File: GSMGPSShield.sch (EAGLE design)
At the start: 65 parts, among them IC1 RT8289, IC2 SIM900, J1 SIM Socket, J2 Antenna, J3 Breakout 1, J4 Breakout 2, J5 ARDUINO-SHIELD_R3, Q1 2N7002, Q2 2N7002, Q3 2N7002, Q4 2N7002, Q5 2N7002

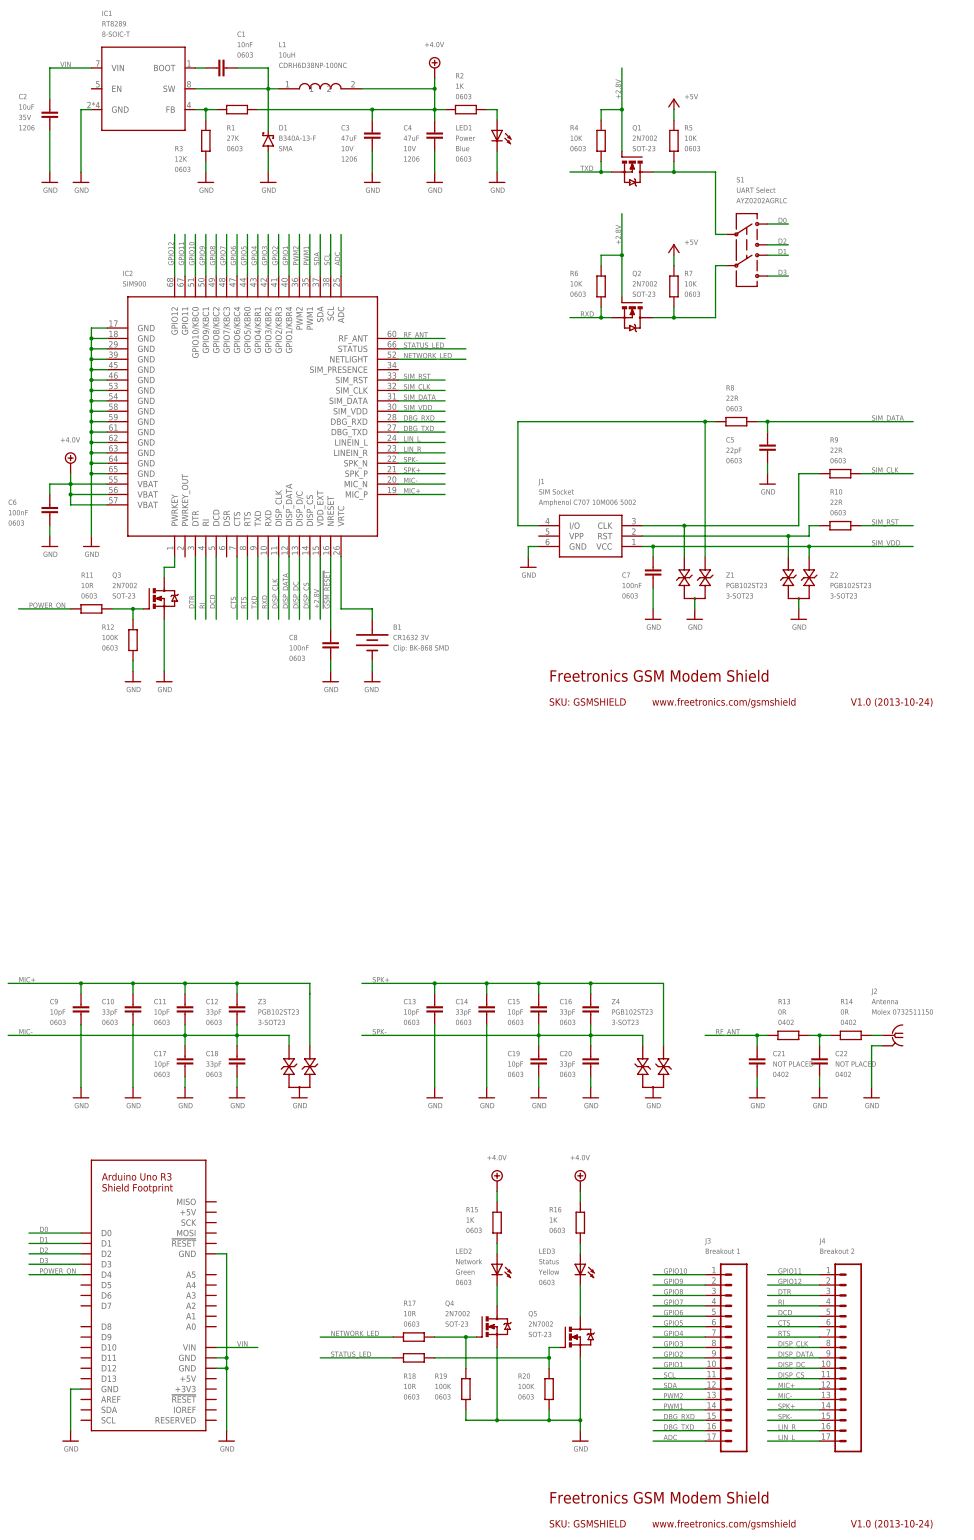
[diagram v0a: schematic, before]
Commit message: changed to SIM908 module, first finished draft
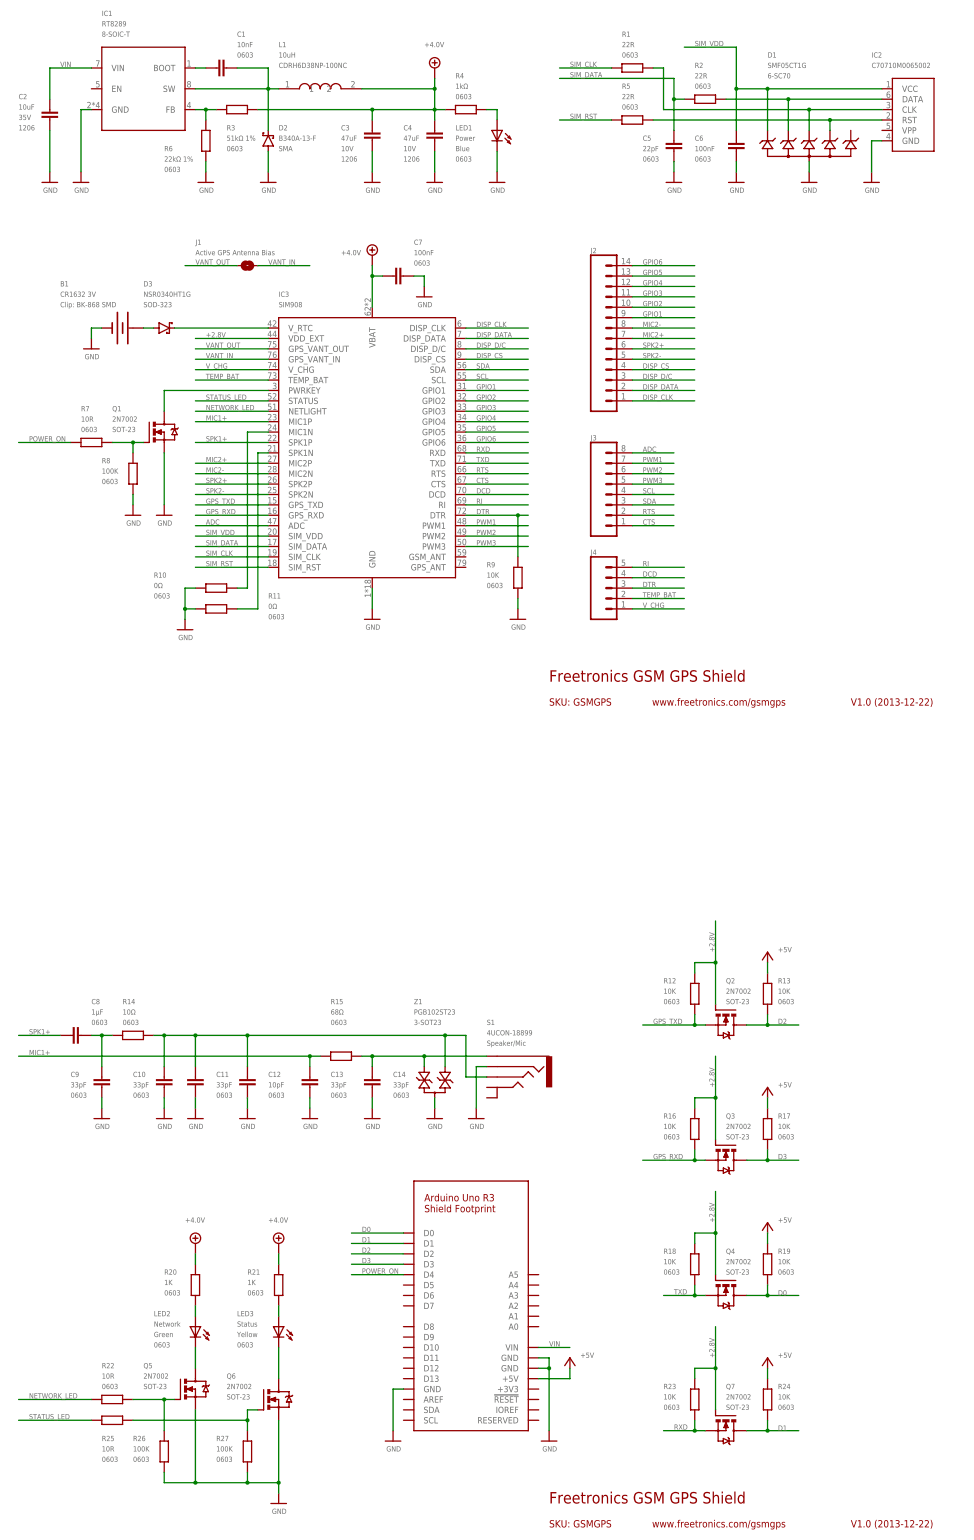
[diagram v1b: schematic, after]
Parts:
- removed C15, C17, C19: 10pF, freetronics-master-v1:CAP0603
- removed C16, C18, C20: 33pF, freetronics-master-v1:CAP0603
- removed C21, C22: NOT PLACED, freetronics-master-v1:CAP0402
- removed Z2, Z3, Z4: PGB102ST23, freetronics-luke:PGB102ST23
- added D2: B340A-13-F, freetronics-luke:SCHOTTKY-SMA
- added D3: NSR0340HT1G, freetronics-luke:SCHOTTKY-SOD323
- added IC3: SIM908, freetronics-luke:SIM908
- added Q6, Q7: 2N7002, freetronics-luke:2N7002
- added R21: 1K, freetronics-master-v1:RESISTOR0603
- added R22, R25: 10R, freetronics-master-v1:RESISTOR0603
- added R23, R24: 10K, freetronics-master-v1:RESISTOR0603
- added R26, R27: 100K, freetronics-master-v1:RESISTOR0603
- C11, C13, C9: value 10pF -> 33pF
- C12: value 33pF -> 10pF
- C8: value 100nF -> 1µF
- D1: value B340A-13-F -> SMF05CT1G; device freetronics-luke:SCHOTTKY-SMA -> freetronics-luke:SMF05CT1G; PACKAGE SMA -> 6-SC70
- IC2: value SIM900 -> C70710M0065002; device ICs_v54:SIM900 -> freetronics-luke:C70710M0065002
- J1: value SIM Socket -> Active GPS Antenna Bias; device SparkFun2:SIMHOLDER3 -> freetronics-luke:SJ; ID Amphenol C707 10M006 5002 -> (none)
- J2: value Antenna -> M14; device con-coax:SMA-142-0701-881/886 -> freetronics-master-v1:M14; ID Molex 0732511150 -> (none)
- J3: value Breakout 1 -> (none); device freetronics-master-v1:M17 -> freetronics-master-v1:M08STD
- J4: value Breakout 2 -> (none); device freetronics-master-v1:M17 -> freetronics-master-v1:M05PTH
- J5: value ARDUINO-SHIELD_R3 -> ARDUINO-SHIELD_R3_NOISP; device freetronics-luke:ARDUINO-SHIELD_R3 -> freetronics-luke:ARDUINO-SHIELD_R3_NOISP
- R1: value 27K -> 22R
- R10: value 22R -> 0Ω
- R11: value 10R -> 0Ω
- R12, R19: value 100K -> 10K
- R13: value 0R -> 10K; device freetronics-master-v1:RESISTOR0402 -> freetronics-master-v1:RESISTOR0603; PACKAGE 0402 -> 0603
- R14: value 0R -> 10Ω; device freetronics-master-v1:RESISTOR0402 -> freetronics-master-v1:RESISTOR0603; PACKAGE 0402 -> 0603
- R15: value 1K -> 68Ω
- R16: value 1K -> 10K
- R17, R18: value 10R -> 10K
- R2: value 1K -> 22R
- R20: value 100K -> 1K
- R3: value 12K -> 51kΩ 1%
- R4: value 10K -> 1kΩ
- R5: value 10K -> 22R
- R6: value 10K -> 22kΩ 1%
- R7: value 10K -> 10R
- R8: value 22R -> 100K
- R9: value 22R -> 10K
- S1: value UART Select -> 4UCON-18899; device freetronics-master-v1:SWITCH-DPDTSMD -> freetronics-jon:AUDIO-JACK-4POLE; FOO (none) -> Speaker/Mic; ID AYZ0202AGRLC -> (none)
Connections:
- removed net !GSM_RESET: C8.2, IC2.NRESET
- removed net DBG_RXD: IC2.DBG_RXD, J3.15
- removed net DBG_TXD: IC2.DBG_TXD, J3.16
- removed net DISP_DC: IC2.DISP_D/C, J4.10
- removed net GPIO10: IC2.GPIO10/KBC0, J3.1
- removed net GPIO11: IC2.GPIO11, J4.1
- removed net GPIO12: IC2.GPIO12, J4.2
- removed net GPIO7: IC2.GPIO7/KBC3, J3.4
- removed net GPIO8: IC2.GPIO8/KBC2, J3.3
- removed net GPIO9: IC2.GPIO9/KBC1, J3.2
- removed net LIN_L: IC2.LINEIN_L, J4.17
- removed net LIN_R: IC2.LINEIN_R, J4.16
- removed net MIC+: C10.2, C11.2, C12.2, C9.2, IC2.MIC_P, J4.12, Z3.P$2
- removed net MIC-: C11.1, C12.1, C17.2, C18.2, IC2.MIC_N, J4.13, Z3.P$1
- removed net N$22: J1.RST, R10.2, Z2.P$1
- removed net N$40: J1.CLK, R9.2, Z1.P$1
- removed net N$49: J1.I/O, R8.2, Z1.P$2
- removed net N$6: B1.+, IC2.VRTC
- removed net N$67: IC2.PWRKEY, Q3.D
- removed net N$69: Q3.G, R11.1, R12.2
- removed net N$70: C22.2, R13.2, R14.1
- removed net N$71: J2G1.1, R14.2
- removed net RF_ANT: C21.2, IC2.RF_ANT, R13.1
- removed net RXD_5V: Q2.D, R7.2, S1.5
- removed net SPK+: C13.2, C14.2, C15.2, C16.2, IC2.SPK_P, J4.14, Z4.P$1
- removed net SPK-: C15.1, C16.1, C19.2, C20.2, IC2.SPK_N, J4.15, Z4.P$2
- removed net TXD_5V: Q1.D, R5.2, S1.2
- new net DISP_D/C: IC3.DISP_D/C, J2.3
- new net GPS_RXD: IC3.GPS_RXD, Q3.S, R16.2
- new net GPS_TXD: IC3.GPS_TXD, Q2.S, R12.2
- new net MIC1+: C13.2, IC3.MIC1P, R15.1
- new net MIC2+: IC3.MIC2P, J2.7
- new net MIC2-: IC3.MIC2N, J2.8
- new net N$10: IC3.SPK1N, R11.1
- new net N$11: IC3.MIC1N, R10.1
- new net N$12: D1.K5, IC2.RST, R5.1
- new net N$13: D1.K4, IC2.CLK, R1.1
- new net N$15: D1.K3, IC2.DATA, R2.1
- new net N$16: C14.2, R15.2, S1.1, Z1.P$2
- new net N$17: C10.2, C11.2, C12.2, R14.2, S1.3, Z1.P$1
- new net N$20: C8.1, C9.2, R14.1
- new net N$34: Q1.G, R7.1, R8.2
- new net N$7: D3.K, IC3.V_RTC
- new net N$8: IC3.PWRKEY, Q1.D
- new net N$9: B1.+, D3.A
- new net PWM3: IC3.PWM3, J3.5
- new net SPK1+: C8.2, IC3.SPK1P
- new net SPK2+: IC3.SPK2P, J2.6
- new net SPK2-: IC3.SPK2N, J2.5
- new net TEMP_BAT: IC3.TEMP_BAT, J4.2
- new net VANT_IN: IC3.GPS_VANT_IN, J1.2
- new net VANT_OUT: IC3.GPS_VANT_OUT, J1.1
- new net V_CHG: IC3.V_CHG, J4.1
- net +2.8V: now also IC3.VDD_EXT, Q3.G, Q4.G, Q7.G, R12.1, R16.1, R18.1, R23.1; no longer IC2.VDD_EXT, Q1.G, R4.1, R6.1
- net +4.0V: now also C7.2, IC3.VBAT, R20.1, R21.1, R3.1, R4.1; no longer C6.2, IC2.VBAT@0, IC2.VBAT@1, IC2.VBAT@2, R1.1, R15.1, R16.1, R2.1
- net +5V: now also J5.+5V, R13.1, R17.1, R19.1, R24.1; no longer R5.1, R7.1
- net ADC: now also IC3.ADC, J3.8; no longer IC2.ADC, J3.17
- net CTS: now also IC3.CTS, J3.1; no longer IC2.CTS, J4.6
- net D0: now also Q4.D, R19.2; no longer S1.1
- net D1: now also Q7.D, R24.2; no longer S1.4
- net D2: now also Q2.D, R13.2; no longer S1.3
- net D3: now also Q3.D, R17.2; no longer S1.6
- net DCD: now also IC3.DCD, J4.4; no longer IC2.DCD, J4.5
- net DISP_CLK: now also IC3.DISP_CLK, J2.1; no longer IC2.DISP_CLK, J4.8
- net DISP_CS: now also IC3.DISP_CS, J2.4; no longer IC2.DISP_CS, J4.11
- net DISP_DATA: now also IC3.DISP_DATA, J2.2; no longer IC2.DISP_DATA, J4.9
- net DTR: now also IC3.DTR, R9.1; no longer IC2.DTR
- net GND: now also C11.1, C12.1, D1.A2, D2.A, IC2.GND, IC3.GND, Q1.S, Q6.S, R10.2, R11.2, R26.1, R27.1, R6.1, R8.1, R9.2, S1.4; no longer C17.1, C18.1, C19.1, C20.1, C21.1, C22.1, C8.1, D1.A, IC2.GND@0, IC2.GND@1, IC2.GND@10, IC2.GND@11, IC2.GND@12, IC2.GND@13, IC2.GND@14, IC2.GND@2, IC2.GND@3, IC2.GND@4, IC2.GND@5, IC2.GND@6, IC2.GND@7, IC2.GND@8, IC2.GND@9, J1.GND, J2G1.GND, J5.GND@2, Q3.S, Q4.S, R12.1, R19.1, R20.1, R3.1, Z2.P$3, Z3.P$3, Z4.P$3
- net GPIO1: now also IC3.GPIO1, J2.9; no longer IC2.GPIO1/KBR4, J3.10
- net GPIO2: now also IC3.GPIO2, J2.10; no longer IC2.GPIO2/KBR3, J3.9
- net GPIO3: now also IC3.GPIO3, J2.11; no longer IC2.GPIO3/KBR2, J3.8
- net GPIO4: now also IC3.GPIO4, J2.12; no longer IC2.GPIO4/KBR1, J3.7
- net GPIO5: now also IC3.GPIO5, J2.13; no longer IC2.GPIO5/KBR0, J3.6
- net GPIO6: now also IC3.GPIO6, J2.14; no longer IC2.GPIO6/KBC4, J3.5
- net N$1: now also R4.2; no longer R2.2
- net N$143: now also D2.K; no longer D1.K
- net N$144: now also R6.2; no longer R1.2
- net N$2: now also Q5.D; no longer Q4.D
- net N$3: now also Q6.D; no longer Q5.D
- net N$4: now also Q5.G, R22.1, R26.2; no longer Q4.G, R17.1, R19.2
- net N$5: now also Q6.G, R25.1, R27.2; no longer Q5.G, R18.1, R20.2
- net N$76: now also R21.2; no longer R16.2
- net N$77: now also R20.2; no longer R15.2
- net NETWORK_LED: now also IC3.NETLIGHT, R22.2; no longer IC2.NETLIGHT, R17.2
- net POWER_ON: now also R7.2; no longer R11.2
- net PWM1: now also IC3.PWM1, J3.7; no longer IC2.PWM1, J3.14
- net PWM2: now also IC3.PWM2, J3.6; no longer IC2.PWM2, J3.13
- net RI: now also IC3.RI, J4.5; no longer IC2.RI, J4.4
- net RTS: now also IC3.RTS, J3.2; no longer IC2.RTS, J4.7
- net RXD: now also IC3.RXD, Q7.S, R23.2; no longer IC2.RXD, Q2.S, R6.2
- net SCL: now also IC3.SCL, J3.4; no longer IC2.SCL, J3.11
- net SDA: now also IC3.SDA, J3.3; no longer IC2.SDA, J3.12
- net SIM_CLK: now also IC3.SIM_CLK, R1.2; no longer IC2.SIM_CLK, R9.1
- net SIM_DATA: now also IC3.SIM_DATA, R2.2; no longer IC2.SIM_DATA, R8.1
- net SIM_RST: now also IC3.SIM_RST, R5.2; no longer IC2.SIM_RST, R10.1
- net SIM_VDD: now also C6.2, D1.K1, IC2.VCC, IC3.SIM_VDD; no longer C7.2, IC2.SIM_VDD, J1.VCC, Z2.P$2
- net STATUS_LED: now also IC3.STATUS, R25.2; no longer IC2.STATUS, R18.2
- net TXD: now also IC3.TXD, Q4.S, R18.2; no longer IC2.TXD, Q1.S, R4.2
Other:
- note added: "Freetronics GSM GPS Shield"
- note added: "SKU: GSMGPS"
- note added: "V1.0 (2013-12-22)"
- note added: "www.freetronics.com/gsmgps"
- note removed: "Freetronics GSM Modem Shield"
- note removed: "SKU: GSMSHIELD"
- note removed: "V1.0 (2013-10-24)"
- note removed: "www.freetronics.com/gsmshield"
- moved on the sheet: B1, C10, C11, C12, C13, C14, C5, C6, C7, C8, C9, LED2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

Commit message: Replaced Greek characters with Latin equivalents
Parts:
- C8: value 1µF -> 1uF
- R10, R11: value 0Ω -> 0R
- R14: value 10Ω -> 10R
- R15: value 68Ω -> 68R
- R3: value 51kΩ 1% -> 51K 1%
- R4: value 1kΩ -> 1K
- R6: value 22kΩ 1% -> 22K 1%
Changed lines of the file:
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@@
 </classes>
 <parts>
-<part name="R6" library="freetronics-master-v1" deviceset="RESISTOR" device="0603" value="22kΩ 1%">
+<part name="R6" library="freetronics-master-v1" deviceset="RESISTOR" device="0603" value="22K 1%">
 <attribute name="PACKAGE" value="0603"/>
 </part>
@@
 </part>
 <part name="U$102" library="freetronics-luke" deviceset="GND" device=""/>
-<part name="R3" library="freetronics-master-v1" deviceset="RESISTOR" device="0603" value="51kΩ 1%">
+<part name="R3" library="freetronics-master-v1" deviceset="RESISTOR" device="0603" value="51K 1%">
 <attribute name="PACKAGE" value="0603"/>
 </part>
@@
 <part name="SUPPLY3" library="supply2" deviceset="+4.1V" device="" value="+4.0V"/>
 <part name="SUPPLY4" library="supply2" deviceset="+4.1V" device="" value="+4.0V"/>
-<part name="R4" library="freetronics-master-v1" deviceset="RESISTOR" device="0603" value="1kΩ">
+<part name="R4" library="freetronics-master-v1" deviceset="RESISTOR" device="0603" value="1K">
 <attribute name="PACKAGE" value="0603"/>
 </part>
@@
 <attribute name="FOO" value="Speaker/Mic"/>
 </part>
-<part name="R10" library="freetronics-master-v1" deviceset="RESISTOR" device="0603" value="0Ω">
-<attribute name="PACKAGE" value="0603"/>
-</part>
-<part name="R11" library="freetronics-master-v1" deviceset="RESISTOR" device="0603" value="0Ω">
+<part name="R10" library="freetronics-master-v1" deviceset="RESISTOR" device="0603" value="0R">
+<attribute name="PACKAGE" value="0603"/>
+</part>
+<part name="R11" library="freetronics-master-v1" deviceset="RESISTOR" device="0603" value="0R">
 <attribute name="PACKAGE" value="0603"/>
 </part>
 <part name="U$9" library="freetronics-luke" deviceset="GND" device=""/>
-<part name="R15" library="freetronics-master-v1" deviceset="RESISTOR" device="0603" value="68Ω">
+<part name="R15" library="freetronics-master-v1" deviceset="RESISTOR" device="0603" value="68R">
 <attribute name="PACKAGE" value="0603"/>
 </part>
@@
 <attribute name="PACKAGE" value="0603"/>
 </part>
-<part name="R14" library="freetronics-master-v1" deviceset="RESISTOR" device="0603" value="10Ω">
+<part name="R14" library="freetronics-master-v1" deviceset="RESISTOR" device="0603" value="10R">
 <attribute name="PACKAGE" value="0603"/>
 </part>
@@
 <attribute name="PACKAGE" value="0603"/>
 </part>
-<part name="C8" library="freetronics-master-v1" deviceset="CAP" device="0603" value="1µF">
-<attribute name="PACKAGE" value="0603"/>
-</part>
+<part name="C8" library="freetronics-master-v1" deviceset="CAP" device="0603" value="1uF">
+<attribute name="PACKAGE" value="0603"/>
+</part>

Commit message: Replaced level shifter FETs with RJU003N03
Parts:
- Q2, Q3, Q4, Q7: value 2N7002 -> RJU003N03 N-MOSFET; device freetronics-luke:2N7002 -> freetronics-jon:MOSFET-NSOT-323
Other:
- moved on the sheet: Q2, Q3, Q4, Q7
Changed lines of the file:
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@@
 </part>
 <part name="U$1" library="freetronics-luke" deviceset="GND" device=""/>
-<part name="Q7" library="freetronics-luke" deviceset="2N7002" device="" value="2N7002">
+<part name="Q7" library="freetronics-jon" deviceset="MOSFET-N" device="SOT-323" value="RJU003N03 N-MOSFET">
 <attribute name="PACKAGE" value="SOT-23"/>
 </part>
@@
 </part>
 <part name="U$5" library="freetronics-luke" deviceset="+5V" device=""/>
-<part name="Q4" library="freetronics-luke" deviceset="2N7002" device="" value="2N7002">
+<part name="Q4" library="freetronics-jon" deviceset="MOSFET-N" device="SOT-323" value="RJU003N03 N-MOSFET">
 <attribute name="PACKAGE" value="SOT-23"/>
 </part>
@@
 </part>
 <part name="U$3" library="freetronics-luke" deviceset="GND" device=""/>
-<part name="Q3" library="freetronics-luke" deviceset="2N7002" device="" value="2N7002">
+<part name="Q3" library="freetronics-jon" deviceset="MOSFET-N" device="SOT-323" value="RJU003N03 N-MOSFET">
 <attribute name="PACKAGE" value="SOT-23"/>
 </part>
@@
 </part>
 <part name="U$4" library="freetronics-luke" deviceset="+5V" device=""/>
-<part name="Q2" library="freetronics-luke" deviceset="2N7002" device="" value="2N7002">
+<part name="Q2" library="freetronics-jon" deviceset="MOSFET-N" device="SOT-323" value="RJU003N03 N-MOSFET">
 <attribute name="PACKAGE" value="SOT-23"/>
 </part>
@@
 <wire x1="177.8" y1="76.2" x2="177.8" y2="78.74" width="0.1524" layer="91"/>
 <pinref part="Q4" gate="G$1" pin="G"/>
-<wire x1="182.88" y1="78.74" x2="182.88" y2="68.58" width="0.1524" layer="91"/>
-<wire x1="177.8" y1="78.74" x2="182.88" y2="78.74" width="0.1524" layer="91"/>
-<wire x1="182.88" y1="78.74" x2="182.88" y2="88.9" width="0.1524" layer="91"/>
-<label x="182.626" y="81.28" size="1.27" layer="95" rot="R90"/>
-<junction x="182.88" y="78.74"/>
+<wire x1="185.42" y1="78.74" x2="185.42" y2="71.12" width="0.1524" layer="91"/>
+<wire x1="177.8" y1="78.74" x2="185.42" y2="78.74" width="0.1524" layer="91"/>
+<wire x1="185.42" y1="78.74" x2="185.42" y2="88.9" width="0.1524" layer="91"/>
+<label x="185.166" y="81.28" size="1.27" layer="95" rot="R90"/>
+<junction x="185.42" y="78.74"/>
 </segment>
 <segment>
@@
 <wire x1="177.8" y1="43.18" x2="177.8" y2="45.72" width="0.1524" layer="91"/>
 <pinref part="Q7" gate="G$1" pin="G"/>
-<wire x1="182.88" y1="45.72" x2="182.88" y2="35.56" width="0.1524" layer="91"/>
-<wire x1="177.8" y1="45.72" x2="182.88" y2="45.72" width="0.1524" layer="91"/>
-<wire x1="182.88" y1="45.72" x2="182.88" y2="55.88" width="0.1524" layer="91"/>
-<label x="182.626" y="48.26" size="1.27" layer="95" rot="R90"/>
-<junction x="182.88" y="45.72"/>
+<wire x1="185.42" y1="45.72" x2="185.42" y2="38.1" width="0.1524" layer="91"/>
+<wire x1="177.8" y1="45.72" x2="185.42" y2="45.72" width="0.1524" layer="91"/>
+<wire x1="185.42" y1="45.72" x2="185.42" y2="55.88" width="0.1524" layer="91"/>
+<label x="185.166" y="48.26" size="1.27" layer="95" rot="R90"/>
+<junction x="185.42" y="45.72"/>
 </segment>
 <segment>
@@
 <wire x1="177.8" y1="142.24" x2="177.8" y2="144.78" width="0.1524" layer="91"/>
 <pinref part="Q2" gate="G$1" pin="G"/>
-<wire x1="182.88" y1="144.78" x2="182.88" y2="134.62" width="0.1524" layer="91"/>
-<wire x1="177.8" y1="144.78" x2="182.88" y2="144.78" width="0.1524" layer="91"/>
-<wire x1="182.88" y1="144.78" x2="182.88" y2="154.94" width="0.1524" layer="91"/>
-<label x="182.626" y="147.32" size="1.27" layer="95" rot="R90"/>
-<junction x="182.88" y="144.78"/>
+<wire x1="185.42" y1="144.78" x2="185.42" y2="137.16" width="0.1524" layer="91"/>
+<wire x1="177.8" y1="144.78" x2="185.42" y2="144.78" width="0.1524" layer="91"/>
+<wire x1="185.42" y1="144.78" x2="185.42" y2="154.94" width="0.1524" layer="91"/>
+<label x="185.166" y="147.32" size="1.27" layer="95" rot="R90"/>
+<junction x="185.42" y="144.78"/>
 </segment>
 <segment>
@@
 <wire x1="177.8" y1="109.22" x2="177.8" y2="111.76" width="0.1524" layer="91"/>
 <pinref part="Q3" gate="G$1" pin="G"/>
-<wire x1="182.88" y1="111.76" x2="182.88" y2="101.6" width="0.1524" layer="91"/>
-<wire x1="177.8" y1="111.76" x2="182.88" y2="111.76" width="0.1524" layer="91"/>
-<wire x1="182.88" y1="111.76" x2="182.88" y2="121.92" width="0.1524" layer="91"/>
-<label x="182.626" y="114.3" size="1.27" layer="95" rot="R90"/>
-<junction x="182.88" y="111.76"/>
-</segment>
-</net>
+<wire x1="185.42" y1="111.76" x2="185.42" y2="104.14" width="0.1524" layer="91"/>
+<wire x1="177.8" y1="111.76" x2="185.42" y2="111.76" width="0.1524" layer="91"/>
+<wire x1="185.42" y1="111.76" x2="185.42" y2="121.92" width="0.1524" layer="91"/>
+<label x="185.166" y="114.3" size="1.27" layer="95" rot="R90"/>
+<junction x="185.42" y="111.76"/>
+</segment>
+</net>
